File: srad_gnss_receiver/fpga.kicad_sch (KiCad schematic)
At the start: 1 part, among them U1 XC7A50T-FTG256

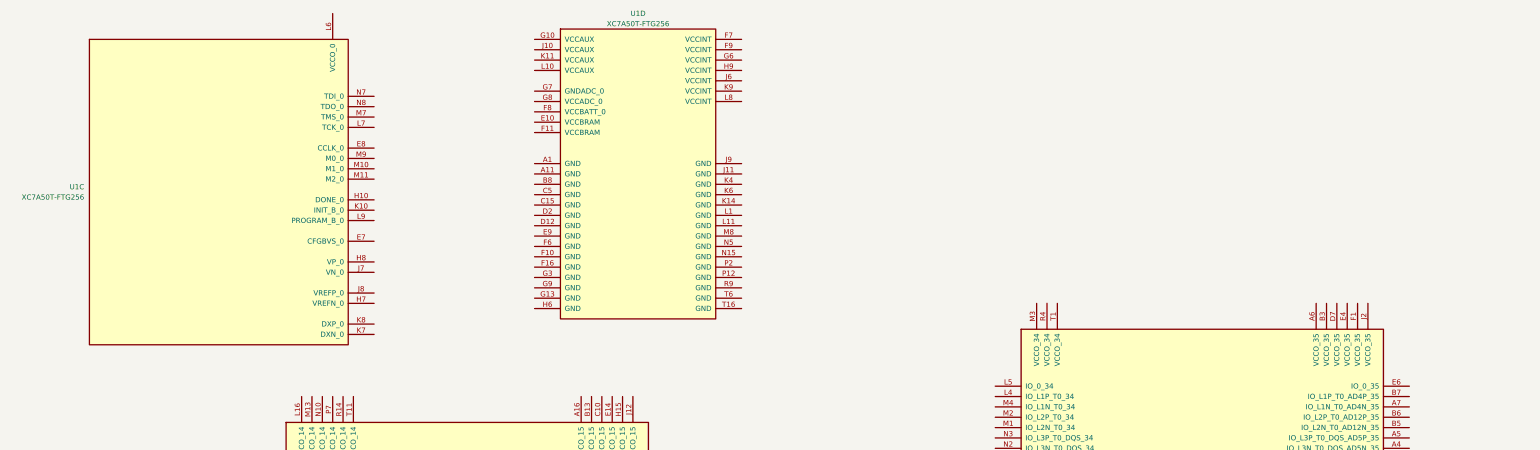
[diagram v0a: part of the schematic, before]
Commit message: add interfaces
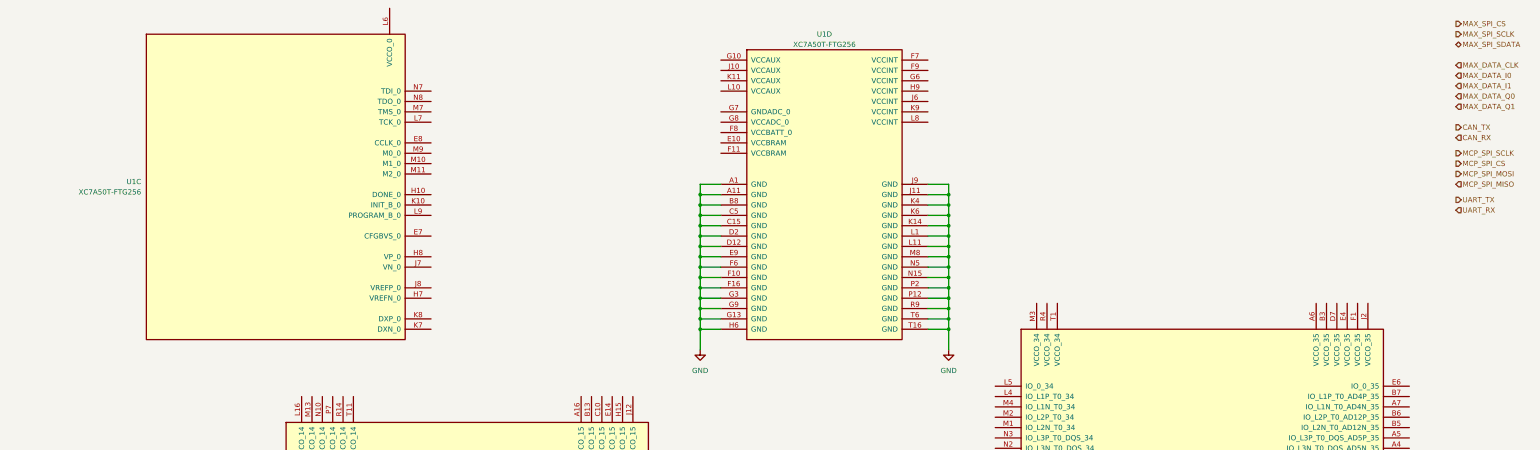
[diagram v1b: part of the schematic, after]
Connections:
- net GND: now reaches U1.A1 (GND)
- net GND: now also U1.A11 (GND), U1.B8 (GND), U1.C15 (GND), U1.C5 (GND), U1.D12 (GND), U1.D2 (GND), U1.E9 (GND), U1.F10 (GND), U1.F16 (GND), U1.F6 (GND), U1.G13 (GND), U1.G3 (GND), U1.G9 (GND), U1.H6 (GND), U1.J11 (GND), U1.J9 (GND), U1.K14 (GND), U1.K4 (GND), U1.K6 (GND), U1.L1 (GND), U1.L11 (GND), U1.M8 (GND), U1.N15 (GND), U1.N5 (GND), U1.P12 (GND), U1.P2 (GND), U1.R9 (GND), U1.T16 (GND), U1.T6 (GND)
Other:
- moved on the sheet: U1C, U1D
